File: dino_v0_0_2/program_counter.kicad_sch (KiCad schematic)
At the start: 20 parts, among them U1 74LS193, U10 74LS02, U11 74LS245, U12 74LS245, U13 74LS245, U14 74LS245, U2 74LS193, U3 74LS193, U36 7400, U4 74LS193

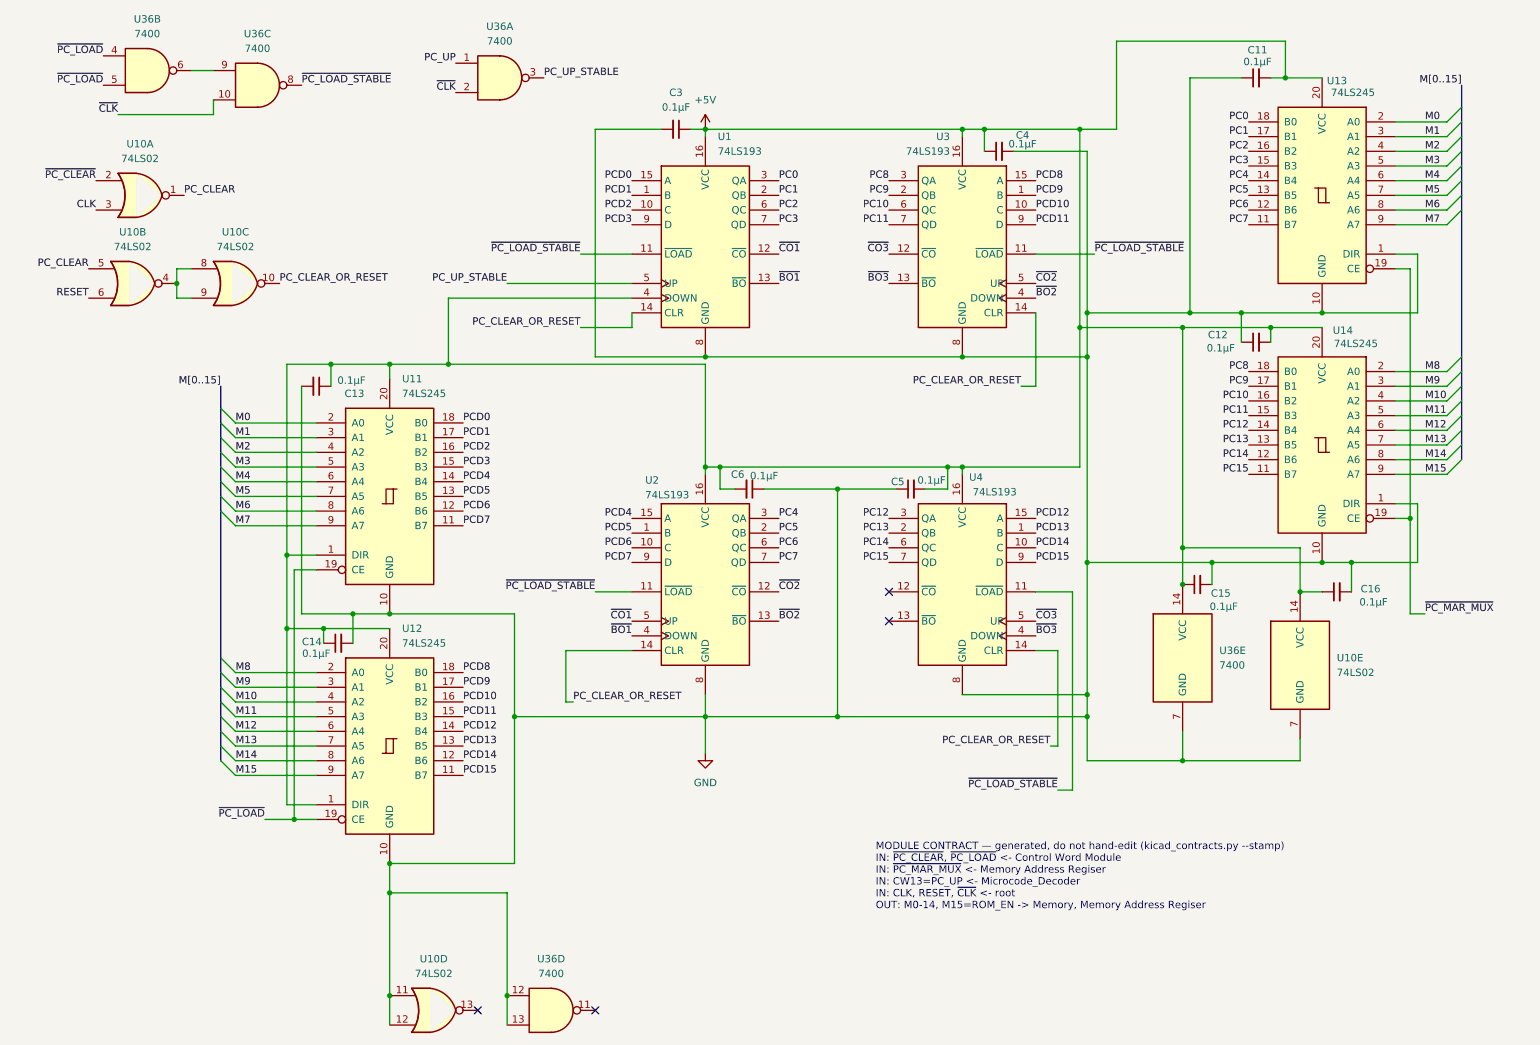
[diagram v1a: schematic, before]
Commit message: fix(schematic): declare matching label sets so aliased nets stay one net
Three board-to-board wires were absent from the generated continuity
checklist, which is the only coverage the netlist->copper step has. A wire
missing from that list is driven by no test and sampled by no test -- the
MAR-lo post-mortem in one sentence.

Cause: cross-sheet connectivity in this design is a naming convention (all
labels are sheet-local; KiCad joins nothing between sheets). kicad_netlist
keys a net on its full label set, joined. When one sheet carries an alias and
another doesn't, the same physical wire gets two keys, both look single-sheet,
and continuity_checklist's cross-sheet filter drops the whole net.

    M15/ROM_EN   mar had both labels, memory had only ROM_EN (on a stub that
                 never joined U24.20's wire), program_counter had only M15.
                 The ROM chip-enable. Missing from every checklist ever
                 generated; survived only because a dead ~CE means the machine
                 never boots, so it self-reports.
    CW17 / CW18  microcode had the bare names, control_word had both. These
                 are U23's only wired outputs -- the entire bank-1 feature
                 rides on them, and both decoders lose their enable if either
                 is unlanded, which at the bench reads like a bad ROM burn.

Fix is in the schematic, not the tool: every sheet touching an aliased net now
declares the same label set. Alias ordering already satisfied the CWnn rule
(`~` sorts after `C`), so CW17/CW18 stay canonical and stay bus members.

  memory           U24.20  ROM_EN -> M15/ROM_EN
  program_counter  U12.9   M15    -> M15/ROM_EN
                   U14.9   M15    -> M15/ROM_EN
  microcode        U23.12  CW17   -> CW17/~{SRC_BANK}
                   U23.13  CW18   -> CW18/~{DST_BANK}

stack_pointer.kicad_sch is UUID churn only, zero connectivity change: the
sheet shipped with 14 duplicate UUIDs (one repeated 5x, consistent with the
four 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
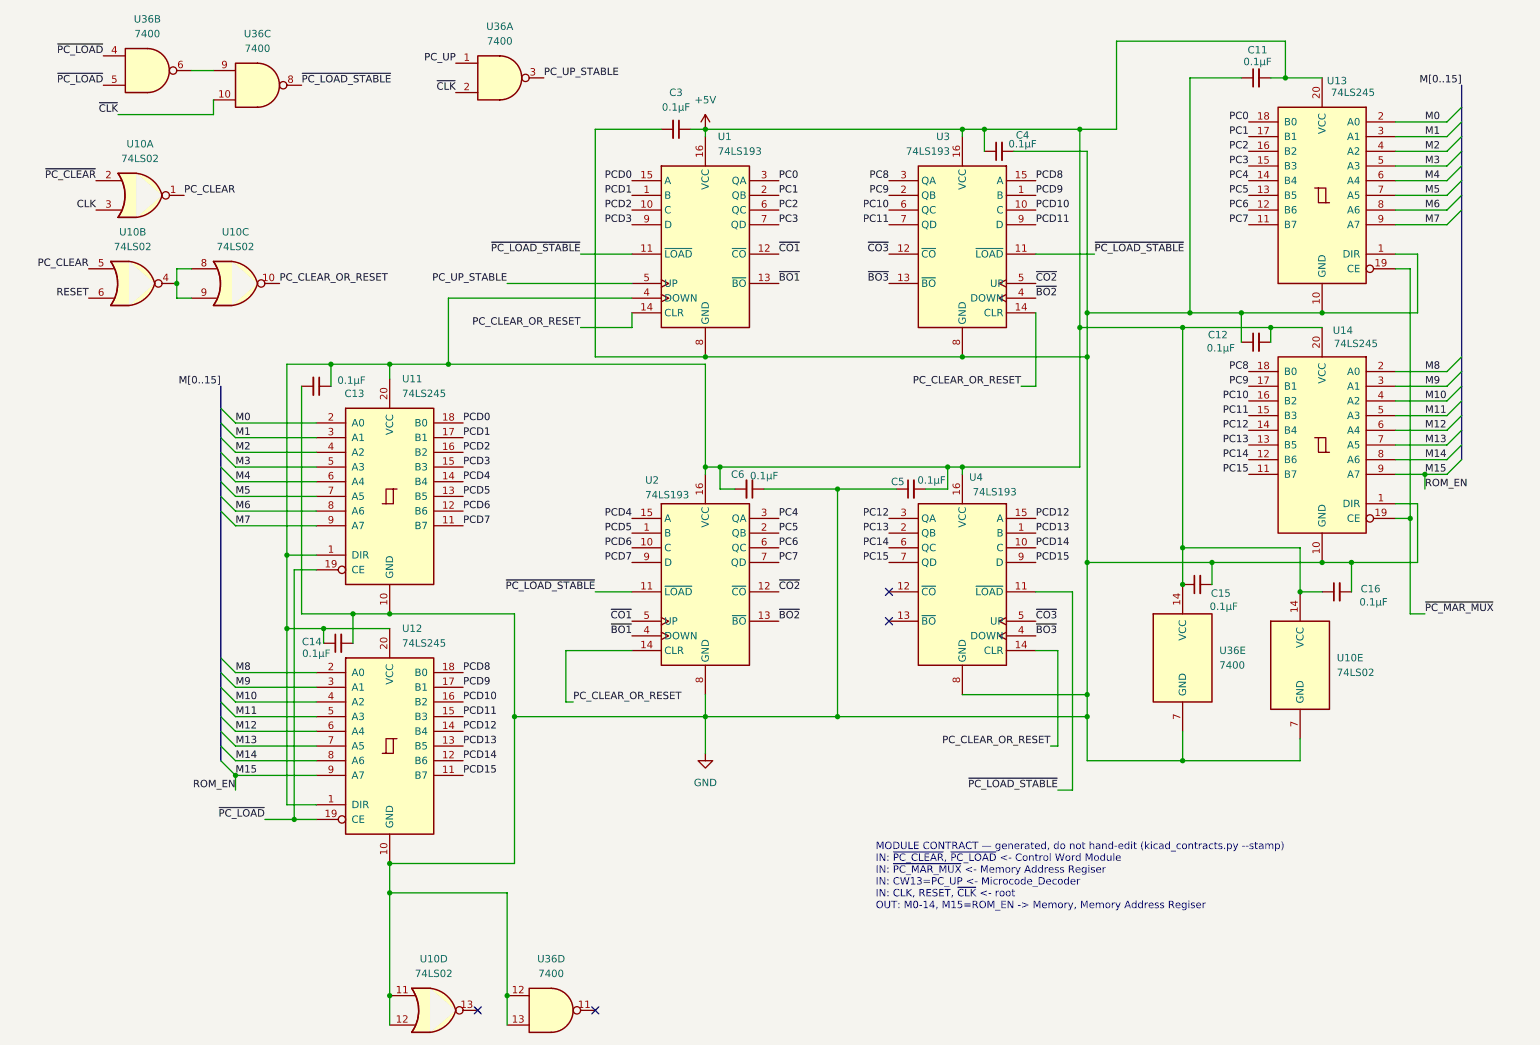
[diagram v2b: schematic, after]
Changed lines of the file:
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@@
 	)
 	(junction
+		(at 48.26 147.32)
+		(diameter 0)
+		(color 0 0 0 0)
+	)
+	(junction
 		(at 63.5 121.92)
 		(diameter 0)
@@
 	)
 	(junction
+		(at 254 95.25)
+		(diameter 0)
+		(color 0 0 0 0)
+	)
+	(junction
 		(at 236.22 67.31)
 		(diameter 0)
@@
 	)
 	(bus_entry
-		(at 45.72 144.78)
-		(size 2.54 2.54)
-		(stroke
-			(width 0)
-			(type default)
-		)
-	)
-	(bus_entry
 		(at 45.72 86.36)
 		(size 2.54 2.54)
@@
 	)
 	(bus_entry
+		(at 45.72 144.78)
+		(size 2.54 2.54)
+		(stroke
+			(width 0)
+			(type default)
+		)
+	)
+	(bus_entry
 		(at 45.72 101.6)
 		(size 2.54 2.54)
@@
 	(wire
 		(pts
+			(xy 254 95.25) (xy 257.81 95.25)
+		)
+		(stroke
+			(width 0)
+			(type default)
+		)
+	)
+	(wire
+		(pts
 			(xy 152.4 97.79) (xy 139.7 97.79)
 		)
@@
 		)
 	)
-	(bus
-		(pts
-			(xy 45.72 142.24) (xy 45.72 144.78)
-		)
-		(stroke
-			(width 0)
-			(type default)
-		)
-	)
 	(wire
 		(pts
@@
 	(wire
 		(pts
+			(xy 48.26 147.32) (xy 62.23 147.32)
+		)
+		(stroke
+			(width 0)
+			(type default)
+		)
+	)
+	(wire
+		(pts
 			(xy 129.54 95.25) (xy 129.54 93.98)
 		)
@@
 	(wire
 		(pts
-			(xy 257.81 95.25) (xy 248.92 95.25)
+			(xy 248.92 95.25) (xy 254 95.25)
 		)
 		(stroke
@@
 	(wire
 		(pts
+			(xy 48.26 147.32) (xy 48.26 149.86)
+		)
+		(stroke
+			(width 0)
+			(type default)
+		)
+	)
+	(wire
+		(pts
 			(xy 257.81 90.17) (xy 248.92 90.17)
 		)
@@
 	(wire
 		(pts
-			(xy 48.26 147.32) (xy 62.23 147.32)
-		)
-		(stroke
-			(width 0)
-			(type default)
-		)
-	)
-	(wire
-		(pts
 			(xy 74.93 119.38) (xy 68.58 119.38)
 		)
@@
 	(wire
 		(pts
+			(xy 254 95.25) (xy 254 97.79)
+		)
+		(stroke
+			(width 0)
+			(type default)
+		)
+	)
+	(wire
+		(pts
 			(xy 105.41 134.62) (xy 106.68 134.62)
 		)
@@
 		)
 	)
+	(bus
+		(pts
+			(xy 45.72 142.24) (xy 45.72 144.78)
+		)
+		(stroke
+			(width 0)
+			(type default)
+		)
+	)
 	(wire
 		(pts
@@
 	)
 	(label "M15"
-		(at 254.0147 95.25 0)
+		(at 254 95.25 0)
 		(effects
 			(font
@@
 		)
 	)
+	(label "ROM_EN"
+		(at 254 97.79 0)
+		(effects
+			(font
+				(size 1.27 1.27)
+			)
+			(justify left bottom)
+		)
+	)
 	(label "PC2"
 		(at 223.52 39.37 180)
@@
 		)
 	)
+	(label "ROM_EN"
+		(at 48.26 149.86 180)
+		(effects
+			(font
+				(size 1.27 1.27)
+			)
+			(justify right bottom)
+		)
+	)
 	(label "M7"
 		(at 48.26 104.14 0)
@@
 	)
 	(label "M15"
-		(at 48.2747 147.32 0)
+		(at 48.26 147.32 0)
 		(effects
 			(font

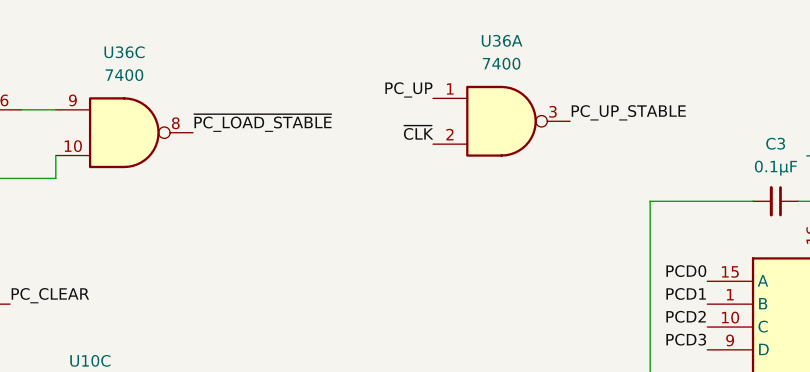
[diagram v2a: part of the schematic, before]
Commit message: schematic: join five aliased nets, and ledger the root-sheet gap
FIVE LIVE WIRES WERE IN THE CHECKLIST'S NO-CONNECT BUCKET, under the
heading "nothing to land and nothing to beep against."

  CW9/SA2           U15.12  <->  U38.7, U40.7
  CW10/SA1          U15.13  <->  U38.6, U40.6, U53.12
  CW11/SA0          U15.15  <->  U38.5, U40.5, U53.13
  CW13/PC_UP        U15.17  <->  U36.1
  CW14/PC_MAR_MUX   U15.18  <->  U54.19, U59.19, U60.11, U60.12

The microcode sheet labelled each net CWnn; the consumer sheet labelled it
SA2 / PC_UP / PC_MAR_MUX. Two label sets, two net keys, both look
sheet-local, and the cross-sheet filter drops the wire -- the M15/ROM_EN
failure, five more times.

alias_splits() could not see it. It keys on a shared BASE label, which is
how it catches CW17 vs CW17/~{SRC_BANK}. CW9 and SA2 share no substring,
so the guard was structurally blind to this shape.

Applied via kicad_gen_sheet.py ops files -- deterministic uuid5, applied
markers, valid s-expression splices -- not hand edits. Every touched sheet
reparses. dino_sheet_contracts.md is UNCHANGED, which confirms the
contracts path (hierarchical sheet pins) was always right and only the
checklist path was blind. unlanded_stubs 20 -> 14; the five now emit as
NEW: with beep partners.

Cosmetic: CW13 on program_counter sits at the same coordinate as PC_UP.
That anchor has no horizontal run, and same-point is the only placement
guaranteed to attach to the right node. Drag apart in KiCad when convenient.

A THIRD BLIND SPOT, FOUND AND LEDGERED RATHER THAN FIXED. net_pins()
walks the ten child sheets and NOT the root sheet:

    alu control_word input_output mar mdr memory microcode
    program_counter registers_a_b stack_pointer      -- no root

Root carries U6 (T-counter), U7/U8 (T decoders), U20 (divider), U27
(clock/reset), U56, U61, Y1, SW2 -- real parts on no child sheet. Their
pins can never reach a continuity checklist, and any child-sheet net
terminating on root is misreported as a no-connect. 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
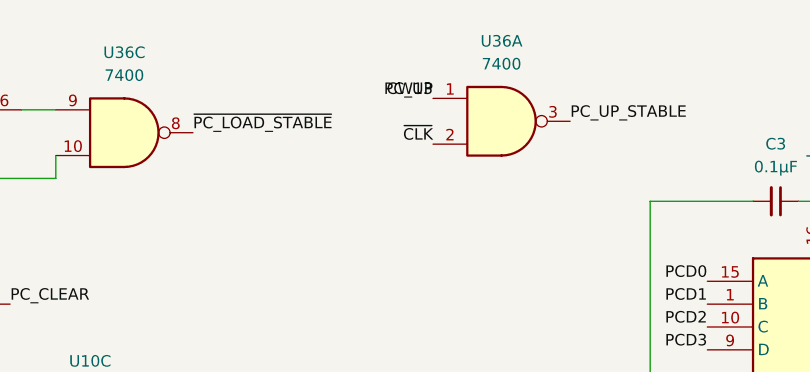
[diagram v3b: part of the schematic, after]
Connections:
- net PC_UP renamed CW13
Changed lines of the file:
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@@
+		)
+	)
+	(label "CW13"
+		(at 86.36 24.13 180)
+		(effects
+			(font
+				(size 1.27 1.27)
+			)
+			(justify right bottom)
 		)
 	)

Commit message: feat: phase D on silicon — the machine executes from RAM
PROG_ramexec returns 0x6E. The PC has been above 0x7FFF and FETCH_RAM has
been high, both for the first time in this machine's life.

The missing condition was never "is this a fetch." ~ROM_OUT is asserted for
every src=ROM — opcode fetch, LDAI's immediate, LDA/STA/JMP/CALL operand
bytes — so an instruction living in RAM must read its operands from RAM
too. The condition is "a ROM-side read was requested, but the address is
above 0x7FFF":

    FETCH_RAM = NOR(~ROM_OUT, ~RAM_EN)

Six gate sections, no new IC. All six were free on U22/U37/U39, already in
sockets on the MDR board, where ~ROM_OUT and ~RAM_OUT already sit feeding
READS_IDLE. Only ~RAM_EN had to be brought in.

    U22 g3   FETCH_RAM     = NOR(~ROM_OUT, ~RAM_EN)
    U22 g4   ROM_BUF_ON    = NOR(~ROM_OUT, FETCH_RAM)
    U37 inv4 ~{FETCH_RAM}
    U37 inv6 ~{ROM_BUF_EN} = OR(~ROM_OUT, FETCH_RAM)   -> U19.19
    U37 inv5 ~{RAM_OE_G}   = AND(~RAM_OUT, ~FETCH_RAM) -> U26.22 + U51.9
    U39 g4   RAM_OE_ON     = NAND(~RAM_OUT, ~FETCH_RAM)

Two pin lifts on the memory board, eleven wires. U24.22 stays on ~ROM_OUT:
U24's own ~CE = M15 already deselects the ROM chip at RAM addresses.

Gating ~RAM_OUT upstream is what keeps this at six gates rather than eight.
U51 is a 7400 computing ~RAM_MDR_EN = AND(~RAM_OUT, ~WRITE_DIR), so one
gate on ~RAM_OUT moves both the RAM chip's ~OE and its buffer's ~CE.

Re-proved before building: all 15 src=ROM microcode rows carry mux_pc=True,
FETCH included, and FILL is src=NONE. A ROM-side read can now land in RAM,
so the standing "ROM reads are exempt from the src=RAM -> MAR loop" rule was
no longer free. It holds — MAR never drives M during a ROM-side read, and a
runaway opcode cannot open the loop either.

The witness is not permutation-blind. If the fetch had still come from ROM,
PC=0x9000 presents A0-A14 = 0x1000 to U24, which is 0xFF fill, which is
HALT, so the poison would have survived as 0xFF. 0x6E is 0x8B - 0x1D,
compu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
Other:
- note added: "MODULE CONTRACT — generated, do not hand-edit (kicad_contracts.py --stamp) IN: ~{PC_CLEAR}, ~{PC_LOAD} <- Control Word Module IN: ~{PC_MAR_MUX} <- Memory Address Regiser IN: CW13=PC_UP <- Microcode_Decoder IN: CLK, RESET, ~{CLK} <- root OUT: PC0-15 -> Memory Data Register OUT: M0-14, M15=ROM_EN -> Memory, Memory Address Regiser"
- note removed: "MODULE CONTRACT — generated, do not hand-edit (kicad_contracts.py --stamp) IN: ~{PC_CLEAR}, ~{PC_LOAD} <- Control Word Module IN: ~{PC_MAR_MUX} <- Memory Address Regiser IN: CW13=PC_UP <- Microcode_Decoder IN: CLK, RESET, ~{CLK} <- root OUT: M0-14, M15=ROM_EN -> Memory, Memory Address Regiser"
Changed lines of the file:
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@@
 		(comment 4 "A Turing-Complete 8-bit \"Computer\"")
 	)
-	(text "MODULE CONTRACT — generated, do not hand-edit (kicad_contracts.py --stamp)\nIN: ~{PC_CLEAR}, ~{PC_LOAD} <- Control Word Module\nIN: ~{PC_MAR_MUX} <- Memory Address Regiser\nIN: CW13=PC_UP <- Microcode_Decoder\nIN: CLK, RESET, ~{CLK} <- root\nOUT: M0-14, M15=ROM_EN -> Memory, Memory Address Regiser"
-		(exclude_from_sim no)
-		(at 159.004 170.688 0)
-		(effects
-			(font
-				(size 1.27 1.27)
-			)
-			(justify left bottom)
-		)
-	)
 	(junction
 		(at 232.41 115.57)
@@
 		)
 	)
+	(text "MODULE CONTRACT — generated, do not hand-edit (kicad_contracts.py --stamp)\nIN: ~{PC_CLEAR}, ~{PC_LOAD} <- Control Word Module\nIN: ~{PC_MAR_MUX} <- Memory Address Regiser\nIN: CW13=PC_UP <- Microcode_Decoder\nIN: CLK, RESET, ~{CLK} <- root\nOUT: PC0-15 -> Memory Data Register\nOUT: M0-14, M15=ROM_EN -> Memory, Memory Address Regiser"
+		(exclude_from_sim no)
+		(at 159.004 170.688 0)
+		(effects
+			(font
+				(size 1.27 1.27)
+			)
+			(justify left bottom)
+		)
+	)

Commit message: feat: phase E step A -- the 16K I/O window, in schematic
Carves 0x4000-0x7FFF out of ROM space and publishes a bus. The ROM now
answers 0x0000-0x3FFF only; the window decodes to no core chip, so W
reads its park -- 0xFF, which is HALT.

TWO NEW PACKAGES, both on the memory board:

  U74 '00  ~{M14}      = NAND(M14, M14)
           ~{ROM_SEL}  = NAND(~{RAM_EN}, ~{M14})
           ~{RAM_OE_G} = NAND(RAM_OE_ON, M15)
           ~{IO_SEL}   = NAND(~{RAM_EN}, M14)
  U75 '32  ~{IO_RD}    = OR(~{IO_SEL}, READS_IDLE)
           ~{IO_WR}    = OR(~{IO_SEL}, ~{RAM_WRITE_EN})
           RESET_B     = OR(RESET, GND)
           ~{IO_RD_Q}  = OR(~{IO_RD}, CLK)

Eight copper changes: U24.20 and U22.12 to ~{ROM_SEL}, U26.22/U51.9 fed
from U74 g3, U39.10 to ~{IO_RD}, U37.10 and U28.7 unlanded, U37.11 to
GND. Park: R4-R8 + R25-R27, 4.7k on W0-7. CLK crosses through R3, 100R,
source end -- the R2 treatment.

IN RETIRES. ~{SW_OUT} has zero pins project-wide. SWITCH-GATE1's enables
are strapped +5V until card zero drives them from an address decode.

THE ROM_EN ALIAS IS DELETED. Once U24.20 moved, ROM_EN named a net with
no ROM consumer. Deleting it half-way SPLIT the net and alias_splits()
caught it mid-edit -- M15: ['M15', 'M15/ROM_EN'], the exact two-key
failure that once cost this project the ROM chip-enable on every
continuity checklist ever generated.

CLK WAS A FOURTH CROSSING THE SPEC DID NOT CARRY. Census: 15 CLK pins,
none on the memory board; ~{CLK} at U51.4 is the wrong polarity and both
new packages are full. SECTION 1's cost table predated the read-term
split that spent U75 g4, so memory is +4 and MDR is +4 -- the wire margin
is zero. Ruled: stay on memory, the output-load argument still holds.

SWITCH-GATE1/SW1/R17-R24/C48 move to their own input.kicad_sch so the
DIP card is modelled as a card. No renumbering: 168 designators
unchanged, --since reports annotate=0.

TOOLING RECONCILED TO THE DESIGN, not the reverse:
  test_continuity_completeness  M15_PINS U24.20 -> U74.10; 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
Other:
- note added: "MODULE CONTRACT — generated, do not hand-edit (kicad_contracts.py --stamp) IN: ~{PC_CLEAR}, ~{PC_LOAD} <- Control Word Module IN: ~{PC_MAR_MUX} <- Memory Address Regiser IN: CW13=PC_UP <- Microcode_Decoder IN: CLK, RESET, ~{CLK} <- root OUT: PC0-15 -> Memory Data Register OUT: M0-15 -> Memory, Memory Address Regiser"
- note removed: "MODULE CONTRACT — generated, do not hand-edit (kicad_contracts.py --stamp) IN: ~{PC_CLEAR}, ~{PC_LOAD} <- Control Word Module IN: ~{PC_MAR_MUX} <- Memory Address Regiser IN: CW13=PC_UP <- Microcode_Decoder IN: CLK, RESET, ~{CLK} <- root OUT: PC0-15 -> Memory Data Register OUT: M0-14, M15=ROM_EN -> Memory, Memory Address Regiser"
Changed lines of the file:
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@@
 	)
 	(junction
-		(at 48.26 147.32)
-		(diameter 0)
-		(color 0 0 0 0)
-	)
-	(junction
 		(at 63.5 121.92)
 		(diameter 0)
@@
 	)
 	(junction
-		(at 254 95.25)
-		(diameter 0)
-		(color 0 0 0 0)
-	)
-	(junction
 		(at 236.22 67.31)
 		(diameter 0)
@@
 	(wire
 		(pts
-			(xy 254 95.25) (xy 257.81 95.25)
-		)
-		(stroke
-			(width 0)
-			(type default)
-		)
-	)
-	(wire
-		(pts
 			(xy 152.4 97.79) (xy 139.7 97.79)
 		)
@@
 	(wire
 		(pts
-			(xy 248.92 95.25) (xy 254 95.25)
+			(xy 248.92 95.25) (xy 257.81 95.25)
 		)
 		(stroke
@@
 	(wire
 		(pts
-			(xy 48.26 147.32) (xy 48.26 149.86)
-		)
-		(stroke
-			(width 0)
-			(type default)
-		)
-	)
-	(wire
-		(pts
 			(xy 257.81 90.17) (xy 248.92 90.17)
 		)
@@
 	(wire
 		(pts
-			(xy 254 95.25) (xy 254 97.79)
-		)
-		(stroke
-			(width 0)
-			(type default)
-		)
-	)
-	(wire
-		(pts
 			(xy 105.41 134.62) (xy 106.68 134.62)
 		)
@@
 		)
 	)
-	(label "ROM_EN"
-		(at 254 97.79 0)
-		(effects
-			(font
-				(size 1.27 1.27)
-			)
-			(justify left bottom)
-		)
-	)
 	(label "PC2"
 		(at 223.52 39.37 180)
@@
 		)
 	)
-	(label "ROM_EN"
-		(at 48.26 149.86 180)
-		(effects
-			(font
-				(size 1.27 1.27)
-			)
-			(justify right bottom)
-		)
-	)
 	(label "M7"
 		(at 48.26 104.14 0)
@@
 		)
 	)
-	(text "MODULE CONTRACT — generated, do not hand-edit (kicad_contracts.py --stamp)\nIN: ~{PC_CLEAR}, ~{PC_LOAD} <- Control Word Module\nIN: ~{PC_MAR_MUX} <- Memory Address Regiser\nIN: CW13=PC_UP <- Microcode_Decoder\nIN: CLK, RESET, ~{CLK} <- root\nOUT: PC0-15 -> Memory Data Register\nOUT: M0-14, M15=ROM_EN -> Memory, Memory Address Regiser"
+	(text "MODULE CONTRACT — generated, do not hand-edit (kicad_contracts.py --stamp)\nIN: ~{PC_CLEAR}, ~{PC_LOAD} <- Control Word Module\nIN: ~{PC_MAR_MUX} <- Memory Address Regiser\nIN: CW13=PC_UP <- Microcode_Decoder\nIN: CLK, RESET, ~{CLK} <- root\nOUT: PC0-15 -> Memory Data Register\nOUT: M0-15 -> Memory, Memory Address Regiser"
 		(exclude_from_sim no)
 		(at 159.004 170.688 0)
